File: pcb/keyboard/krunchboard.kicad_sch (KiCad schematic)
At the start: 197 parts, among them J1 Conn_01x04_Pin, SW1 SW_Push_45deg, SW10 SW_Push_45deg, SW11 SW_Push_45deg, SW12 SW_Push_45deg, SW13 SW_Push_45deg, SW14 SW_Push_45deg, SW15 SW_Push_45deg, SW16 SW_Push_45deg, SW17 SW_Push_45deg, SW18 SW_Push_45deg, SW19 SW_Push_45deg, SW2 SW_Push_45deg, SW20 SW_Push_45deg, SW21 SW_Push_45deg, SW22 SW_Push_45deg, SW23 SW_Push_45deg, SW24 SW_Push_45deg, SW25 SW_Push_45deg, SW26 SW_Push_45deg, SW27 SW_Push_45deg, SW28 SW_Push_45deg, SW29 SW_Push_45deg, SW3 SW_Push_45deg, SW30 SW_Push_45deg, SW31 SW_Push_45deg, SW32 SW_Push_45deg, SW33 SW_Push_45deg, SW34 SW_Push_45deg, SW35 SW_Push_45deg, SW36 SW_Push_45deg, SW37 SW_Push_45deg, SW38 SW_Push_45deg, SW39 SW_Push_45deg, SW4 SW_Push_45deg, SW40 SW_Push_45deg, SW41 SW_Push_45deg, SW42 SW_Push_45deg, SW43 SW_Push_45deg, SW44 SW_Push_45deg, SW45 SW_Push_45deg, SW46 SW_Push_45deg, SW47 SW_Push_45deg, SW48 SW_Push_45deg, SW49 SW_Push_45deg, SW5 SW_Push_45deg, SW50 SW_Push_45deg, SW51 SW_Push_45deg, SW52 SW_Push_45deg, SW53 SW_Push_45deg, SW54 SW_Push_45deg, SW55 SW_Push_45deg, SW56 SW_Push_45deg, SW57 SW_Push_45deg, SW58 SW_Push_45deg, SW59 SW_Push_45deg, SW6 SW_Push_45deg, SW60 SW_Push_45deg, SW61 SW_Push_45deg, SW62 SW_Push_45deg, SW63 SW_Push_45deg, SW64 SW_Push_45deg, SW65 SW_Push_45deg, SW66 SW_Push_45deg, SW67 SW_Push_45deg, SW68 SW_Push_45deg, SW69 SW_Push_45deg, SW7 SW_Push_45deg, SW70 SW_Push_45deg, SW71 SW_Push_45deg, SW72 SW_Push_45deg, SW73 SW_Push_45deg, SW74 SW_Push_45deg, SW75 SW_Push_45deg, SW76 SW_Push_45deg, SW77 SW_Push_45deg, SW78 SW_Push_45deg, SW79 SW_Push_45deg, SW8 SW_Push_45deg, SW80 SW_Push_45deg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

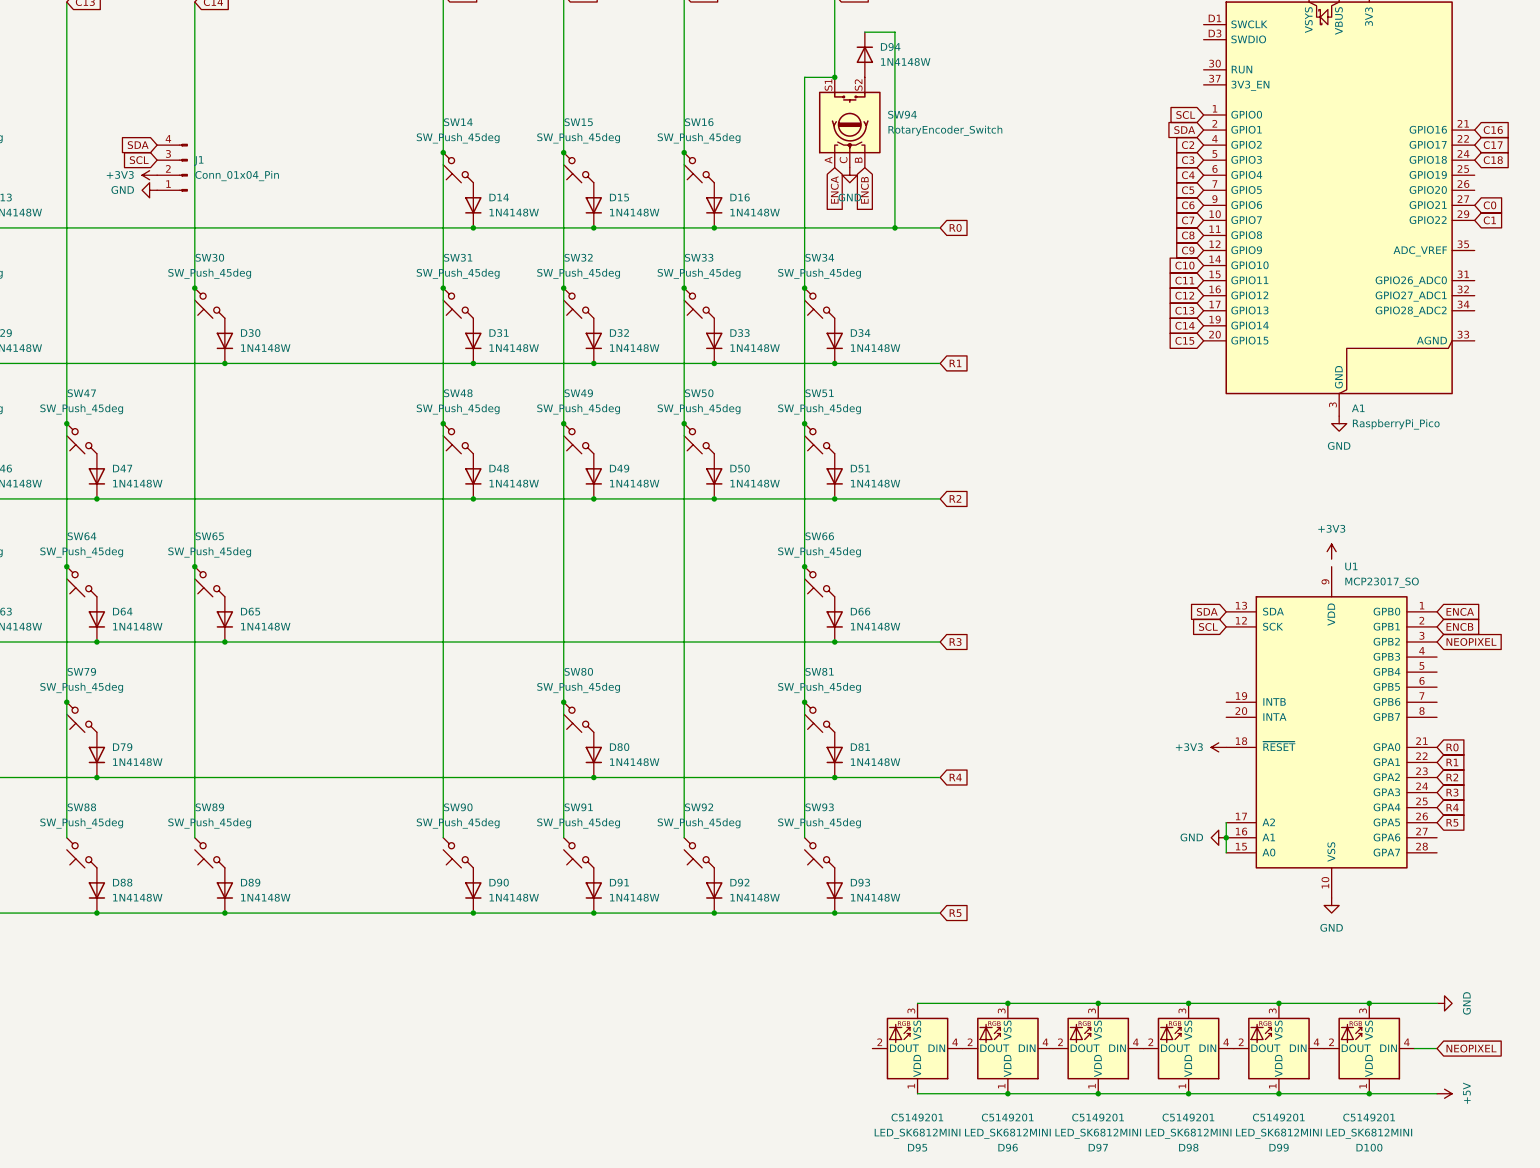
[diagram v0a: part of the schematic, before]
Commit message: pcb files, photos, and added 0.96 oled to firmware
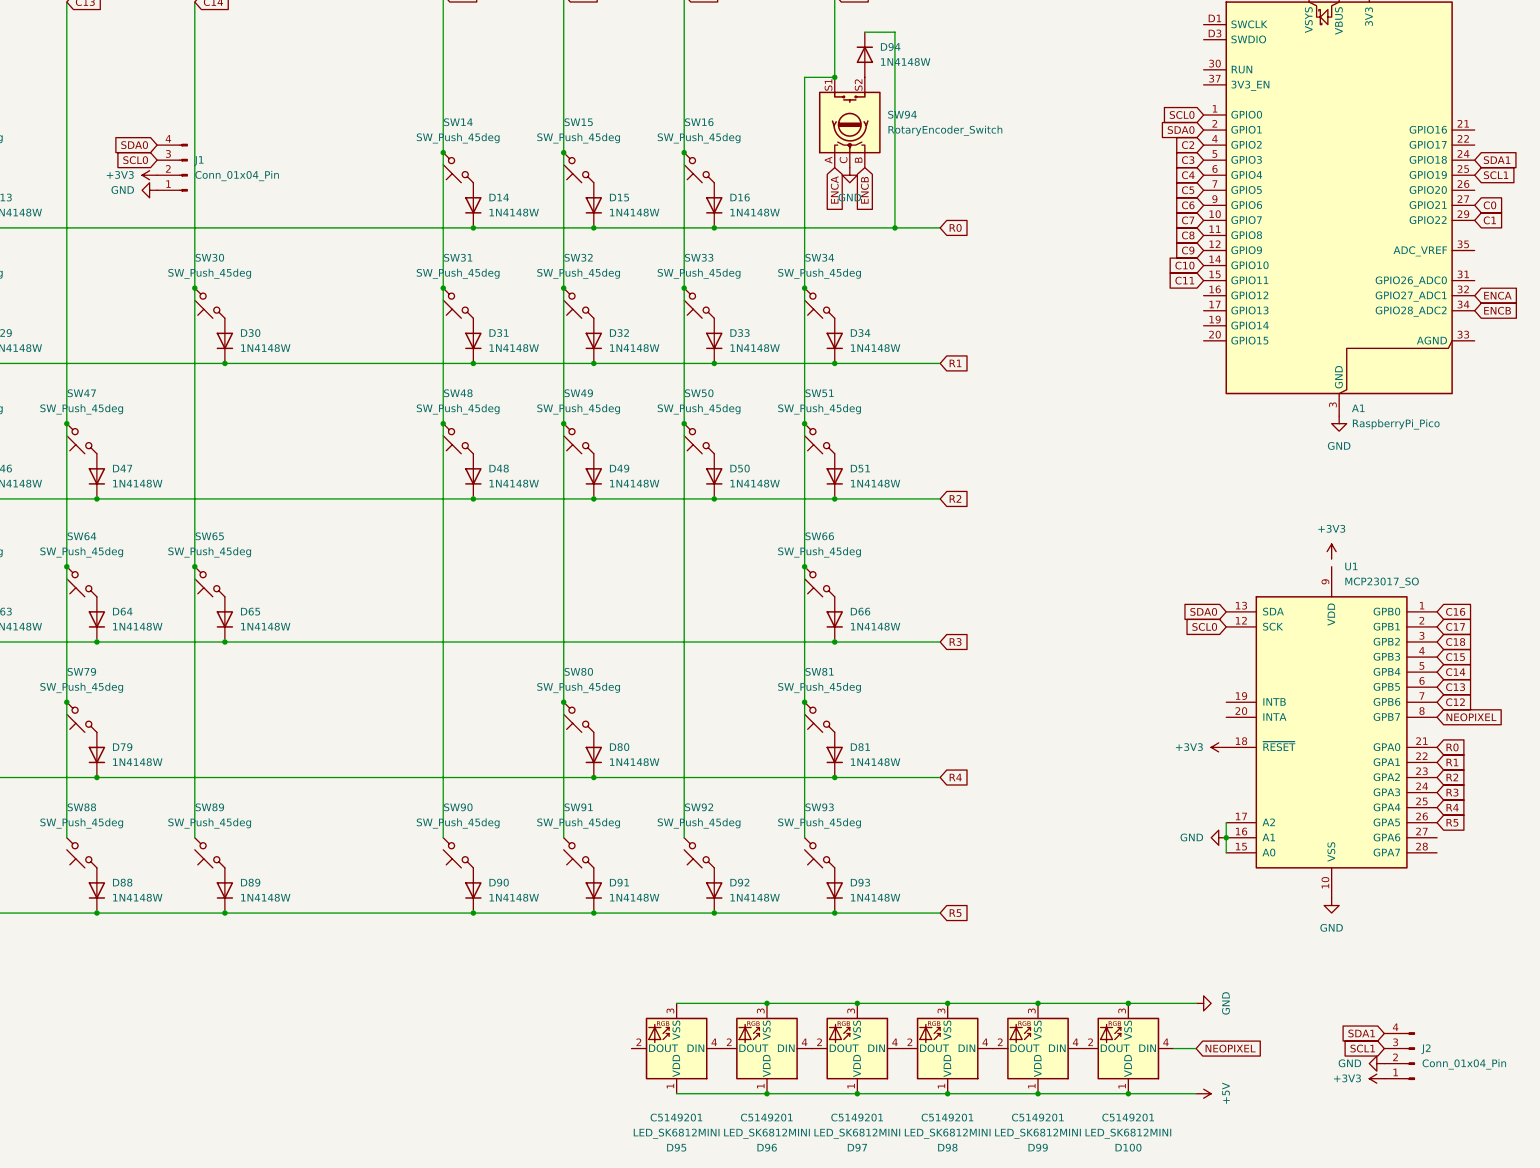
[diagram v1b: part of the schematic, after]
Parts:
- added J2: Conn_01x04_Pin, Connector_PinSocket_2.54mm:PinSocket_1x04_P2.54mm_Vertical, symbol Connector:Conn_01x04_Pin
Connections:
- net +3V3: now also J2.1 (Pin_1)
- net C12: now also U1.7 (GPB6); no longer A1.16 (GPIO12)
- net C13: now also U1.6 (GPB5); no longer A1.17 (GPIO13)
- net C14: now also U1.5 (GPB4); no longer A1.19 (GPIO14)
- net C15: now also U1.4 (GPB3); no longer A1.20 (GPIO15)
- net C16: now also U1.1 (GPB0); no longer A1.21 (GPIO16)
- net C17: now also U1.2 (GPB1); no longer A1.22 (GPIO17)
- net C18: now also U1.3 (GPB2); no longer A1.24 (GPIO18)
- net ENCA: now also A1.32 (GPIO27_ADC1); no longer U1.1 (GPB0)
- net ENCB: now also A1.34 (GPIO28_ADC2); no longer U1.2 (GPB1)
- net GND: now also J2.2 (Pin_2)
- net NEOPIXEL: now also U1.8 (GPB7); no longer U1.3 (GPB2)
- net SCL1: now reaches A1.25 (GPIO19)
- net SCL1: now also J2.3 (Pin_3)
- net SCL renamed SCL0
- net SDA renamed SDA0
- new net SDA1: A1.24 (GPIO18), J2.4 (Pin_4)
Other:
- moved on the sheet: D100, D95, D96, D97, D98, D99

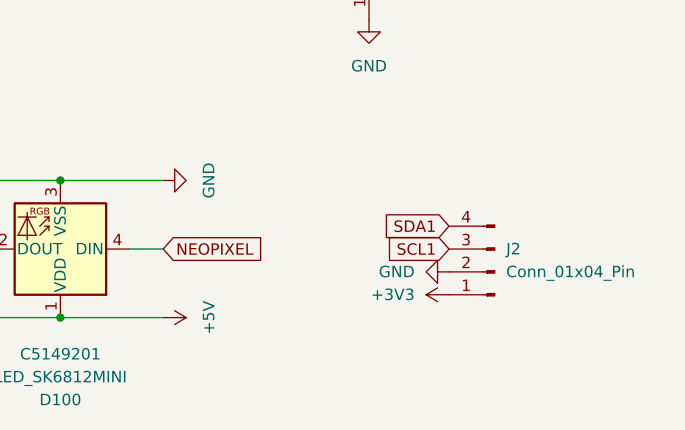
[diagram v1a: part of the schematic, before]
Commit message: swapped 0.96 oled power pins to [GND,VCC,SCL,SDA]
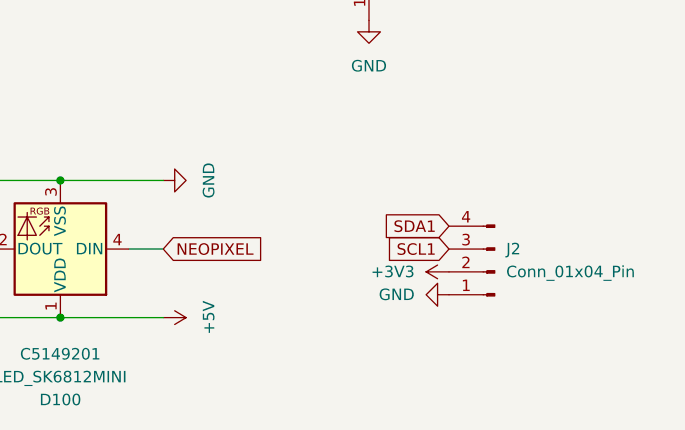
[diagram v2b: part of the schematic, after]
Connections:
- net +3V3: now also J2.2 (Pin_2); no longer J2.1 (Pin_1)
- net GND: now also J2.1 (Pin_1); no longer J2.2 (Pin_2)
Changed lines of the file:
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@@
 	(symbol
 		(lib_id "power:GND")
-		(at 537.21 228.6 270)
+		(at 537.21 231.14 270)
 		(unit 1)
 		(exclude_from_sim no)
@@
 		(fields_autoplaced yes)
 		(property "Reference" "#PWR013"
-			(at 530.86 228.6 0)
+			(at 530.86 231.14 0)
 			(effects
 				(font
@@
 		)
 		(property "Value" "GND"
-			(at 533.4 228.5999 90)
+			(at 533.4 231.1399 90)
 			(effects
 				(font
@@
 		)
 		(property "Footprint" ""
-			(at 537.21 228.6 0)
+			(at 537.21 231.14 0)
 			(effects
 				(font
@@
 		)
 		(property "Datasheet" ""
-			(at 537.21 228.6 0)
+			(at 537.21 231.14 0)
 			(effects
 				(font
@@
 		)
 		(property "Description" "Power symbol creates a global label with name \"GND\" , ground"
-			(at 537.21 228.6 0)
+			(at 537.21 231.14 0)
 			(effects
 				(font
@@
 	(symbol
 		(lib_id "power:+3V3")
-		(at 537.21 231.14 90)
+		(at 537.21 228.6 90)
 		(unit 1)
 		(exclude_from_sim no)
@@
 		(fields_autoplaced yes)
 		(property "Reference" "#PWR012"
-			(at 541.02 231.14 0)
+			(at 541.02 228.6 0)
 			(effects
 				(font
@@
 		)
 		(property "Value" "+3V3"
-			(at 533.4 231.1399 90)
+			(at 533.4 228.5999 90)
 			(effects
 				(font
@@
 		)
 		(property "Footprint" ""
-			(at 537.21 231.14 0)
+			(at 537.21 228.6 0)
 			(effects
 				(font
@@
 		)
 		(property "Datasheet" ""
-			(at 537.21 231.14 0)
+			(at 537.21 228.6 0)
 			(effects
 				(font
@@
 		)
 		(property "Description" "Power symbol creates a global label with name \"+3V3\""
-			(at 537.21 231.14 0)
+			(at 537.21 228.6 0)
 			(effects
 				(font

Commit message: replaced pin sockets with smd version
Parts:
- J1: footprint 0.91-OLED:SSD1306-0.91-OLED-4pin-128x32 -> Connector_PinSocket_2.54mm:PinSocket_1x04_P2.54mm_Vertical_SMD_Pin1Left
- J2: footprint Connector_PinSocket_2.54mm:PinSocket_1x04_P2.54mm_Vertical -> Connector_PinSocket_2.54mm:PinSocket_1x04_P2.54mm_Vertical_SMD_Pin1Left
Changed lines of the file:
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@@
 			)
 		)
-		(property "Footprint" "Connector_PinSocket_2.54mm:PinSocket_1x04_P2.54mm_Vertical"
+		(property "Footprint" "Connector_PinSocket_2.54mm:PinSocket_1x04_P2.54mm_Vertical_SMD_Pin1Left"
 			(at 542.29 228.6 0)
 			(effects
@@
 			)
 		)
-		(property "Footprint" "0.91-OLED:SSD1306-0.91-OLED-4pin-128x32"
+		(property "Footprint" "Connector_PinSocket_2.54mm:PinSocket_1x04_P2.54mm_Vertical_SMD_Pin1Left"
 			(at 335.28 78.74 0)
 			(effects
